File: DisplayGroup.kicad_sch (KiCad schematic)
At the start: 13 parts, among them U1 HT16K33/28

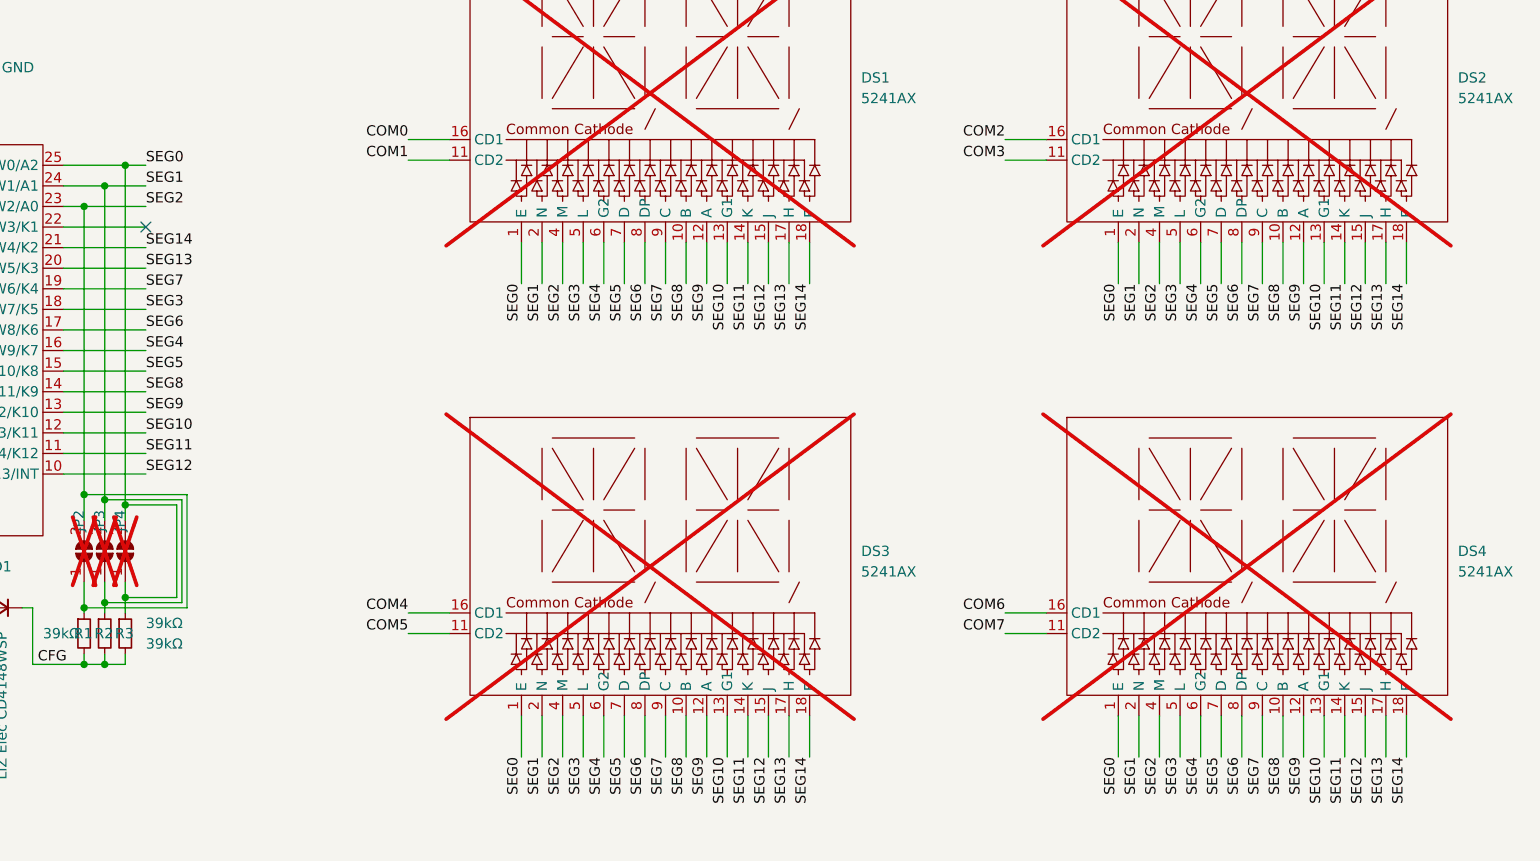
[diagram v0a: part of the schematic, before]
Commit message: Use meaningful segment net names
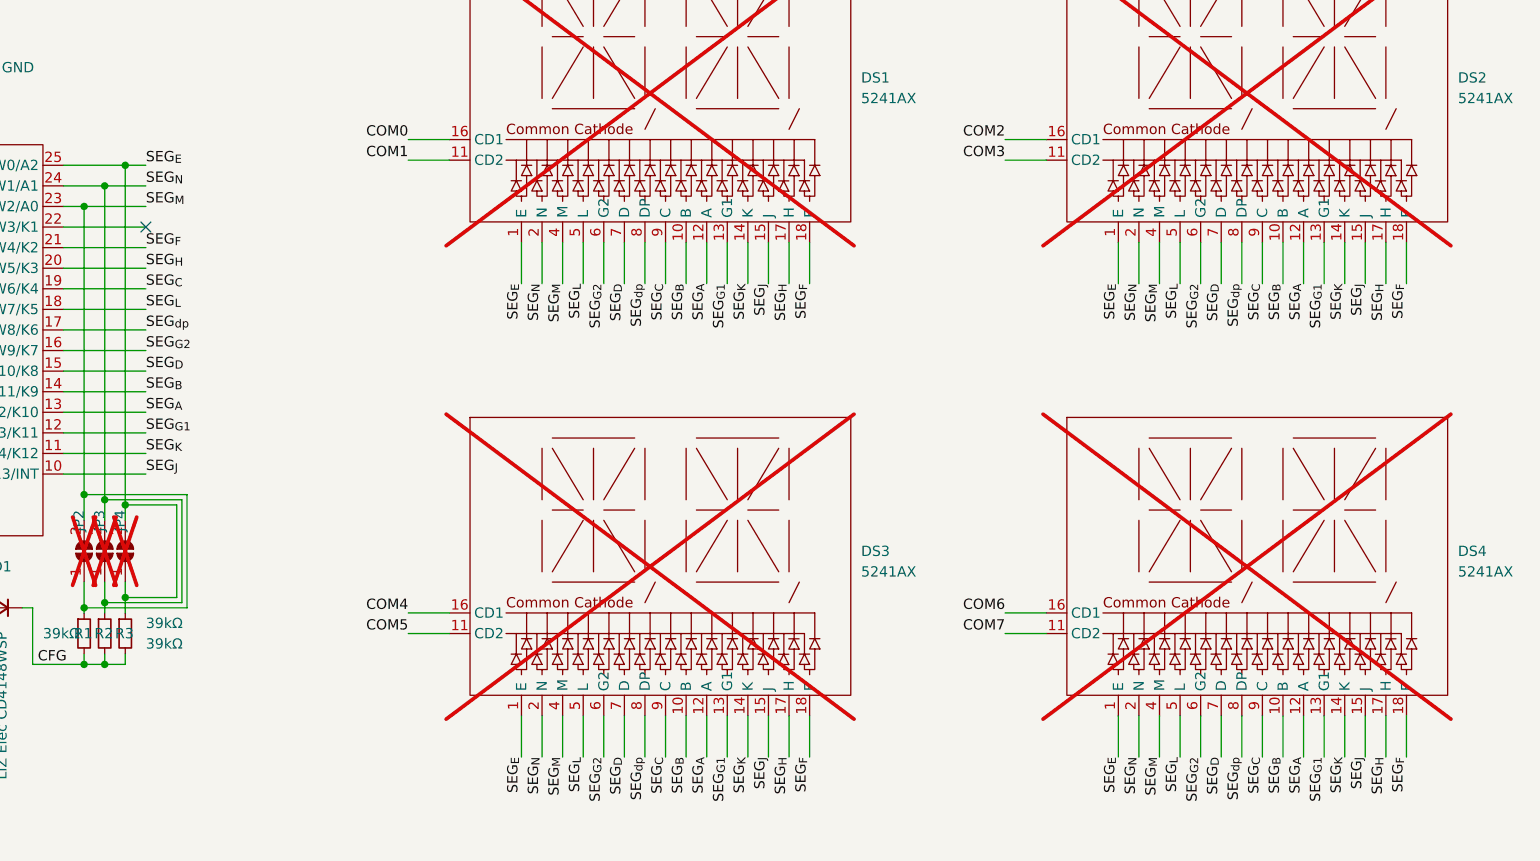
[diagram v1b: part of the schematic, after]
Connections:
- net SEG0 renamed SEG_{E}
- net SEG1 renamed SEG_{N}
- net SEG10 renamed SEG_{G1}
- net SEG11 renamed SEG_{K}
- net SEG12 renamed SEG_{J}
- net SEG13 renamed SEG_{H}
- net SEG14 renamed SEG_{F}
- net SEG2 renamed SEG_{M}
- net SEG3 renamed SEG_{L}
- net SEG4 renamed SEG_{G2}
- net SEG5 renamed SEG_{D}
- net SEG6 renamed SEG_{dp}
- net SEG7 renamed SEG_{C}
- net SEG8 renamed SEG_{B}
- net SEG9 renamed SEG_{A}

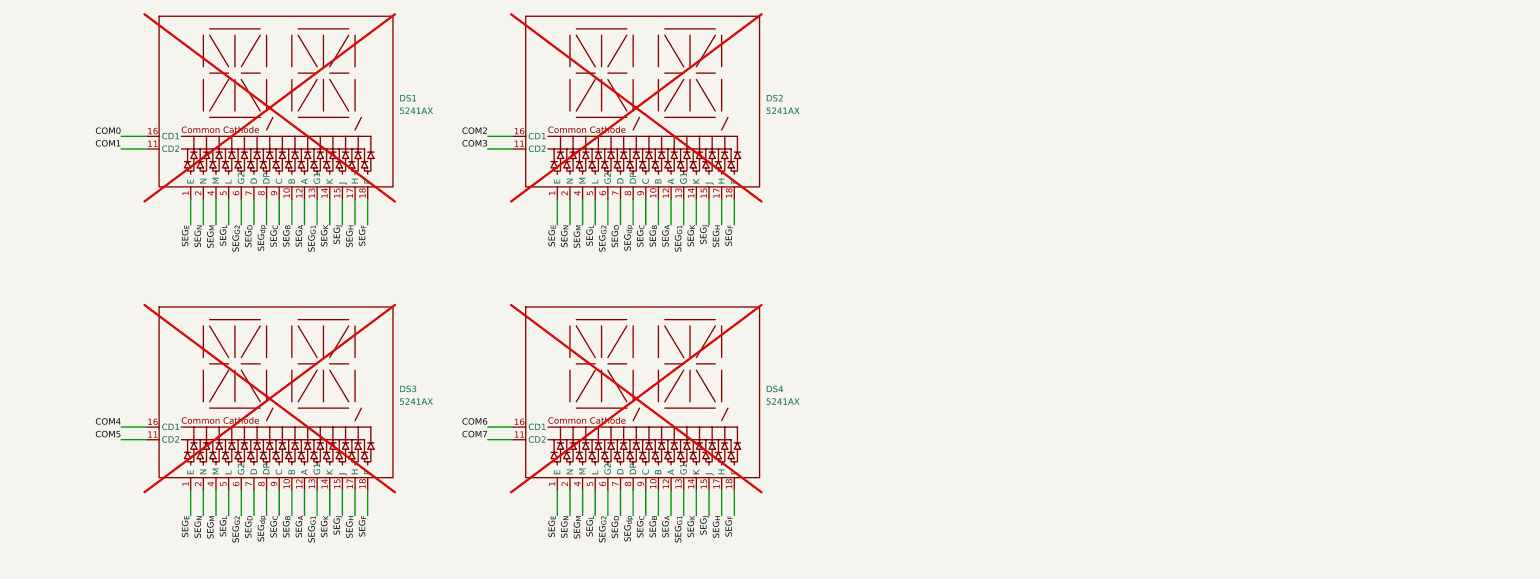
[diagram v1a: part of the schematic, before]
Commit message: Rearrange ROW assignment so digits are scanned consecutively from left to right
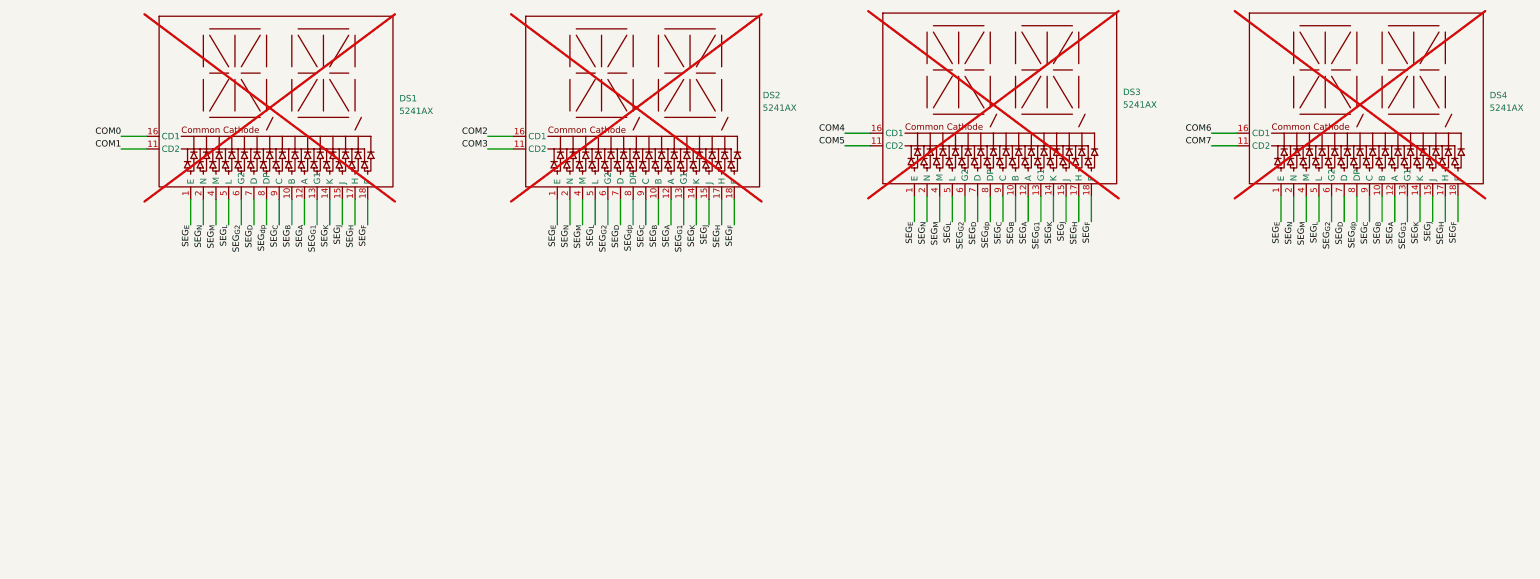
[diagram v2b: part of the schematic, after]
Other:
- moved on the sheet: DS3, DS4

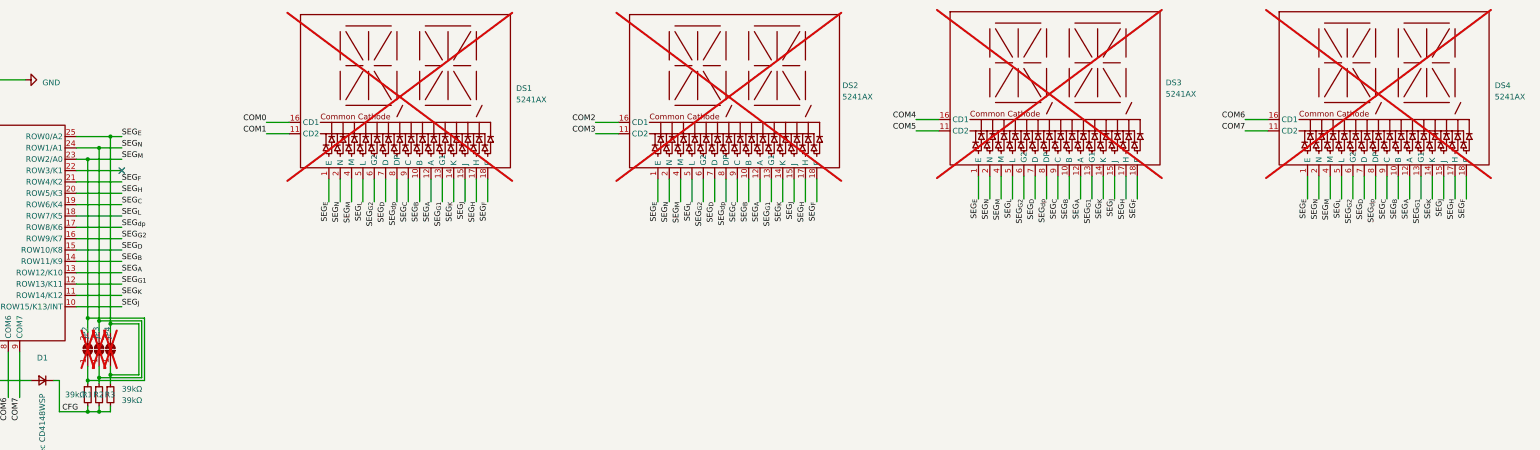
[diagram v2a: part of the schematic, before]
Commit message: Reset usage of flag "do not place"
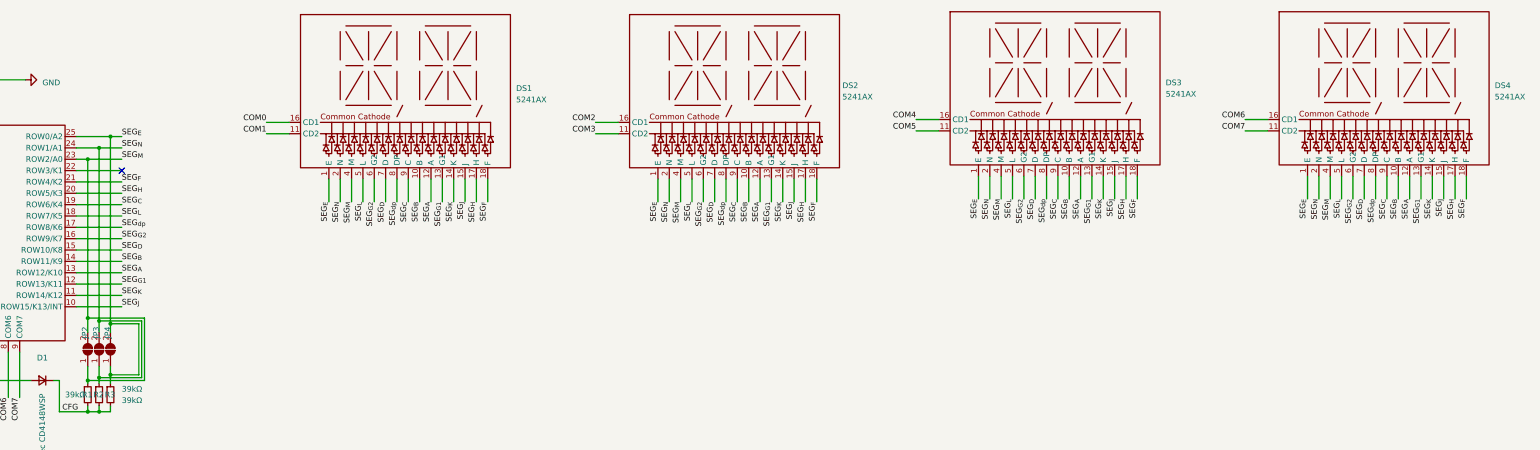
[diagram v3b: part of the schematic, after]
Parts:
- DS1, DS2, DS3, DS4, JP2, JP3, JP4: now fitted
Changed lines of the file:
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@@
   )
   (symbol (lib_id "Jumper:SolderJumper_2_Open") (at 83.82 105.41 90) (unit 1)
-    (in_bom no) (on_board no) (dnp yes)
+    (in_bom no) (on_board no) (dnp no)
     (property "Reference" "JP3" (at 83.185 100.33 0)
       (effects (font (size 1.27 1.27)) (justify right))
@@
   )
   (symbol (lib_id "_ProjectLib:5241AX") (at 298.45 41.275 0) (unit 1)
-    (in_bom yes) (on_board yes) (dnp yes) (fields_autoplaced)
+    (in_bom yes) (on_board yes) (dnp no) (fields_autoplaced)
     (property "Reference" "DS3" (at 322.58 45.72 0)
       (effects (font (size 1.27 1.27)) (justify left))
@@
   )
   (symbol (lib_id "Jumper:SolderJumper_2_Open") (at 86.36 105.41 90) (unit 1)
-    (in_bom no) (on_board no) (dnp yes)
+    (in_bom no) (on_board no) (dnp no)
     (property "Reference" "JP4" (at 85.725 100.33 0)
       (effects (font (size 1.27 1.27)) (justify right))
@@
   )
   (symbol (lib_id "Jumper:SolderJumper_2_Open") (at 81.28 105.41 90) (unit 1)
-    (in_bom no) (on_board no) (dnp yes)
+    (in_bom no) (on_board no) (dnp no)
     (property "Reference" "JP2" (at 80.645 100.33 0)
       (effects (font (size 1.27 1.27)) (justify right))
@@
   )
   (symbol (lib_id "_ProjectLib:5241AX") (at 226.695 41.91 0) (unit 1)
-    (in_bom yes) (on_board yes) (dnp yes) (fields_autoplaced)
+    (in_bom yes) (on_board yes) (dnp no) (fields_autoplaced)
     (property "Reference" "DS2" (at 250.19 46.355 0)
       (effects (font (size 1.27 1.27)) (justify left))
@@
   )
   (symbol (lib_id "_ProjectLib:5241AX") (at 372.11 41.275 0) (unit 1)
-    (in_bom yes) (on_board yes) (dnp yes) (fields_autoplaced)
+    (in_bom yes) (on_board yes) (dnp no) (fields_autoplaced)
     (property "Reference" "DS4" (at 396.24 46.355 0)
       (effects (font (size 1.27 1.27)) (justify left))
@@
   )
   (symbol (lib_id "_ProjectLib:5241AX") (at 153.035 41.91 0) (unit 1)
-    (in_bom yes) (on_board yes) (dnp yes) (fields_autoplaced)
+    (in_bom yes) (on_board yes) (dnp no) (fields_autoplaced)
     (property "Reference" "DS1" (at 177.165 46.99 0)
       (effects (font (size 1.27 1.27)) (justify left))

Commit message: Create schematic PDF
- Define and use slim sheet template
- Define sheet values
- Rearrange schematics for printout
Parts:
- JP2, JP3, JP4: now not fitted
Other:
- moved on the sheet: C1, D1, DS1, DS2, DS3, DS4, R1, R2, R3, U1
